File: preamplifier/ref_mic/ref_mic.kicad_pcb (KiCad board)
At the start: 2 copper layers, 49.8 x 9.8 mm, 28 parts, among them U1 OPAMP

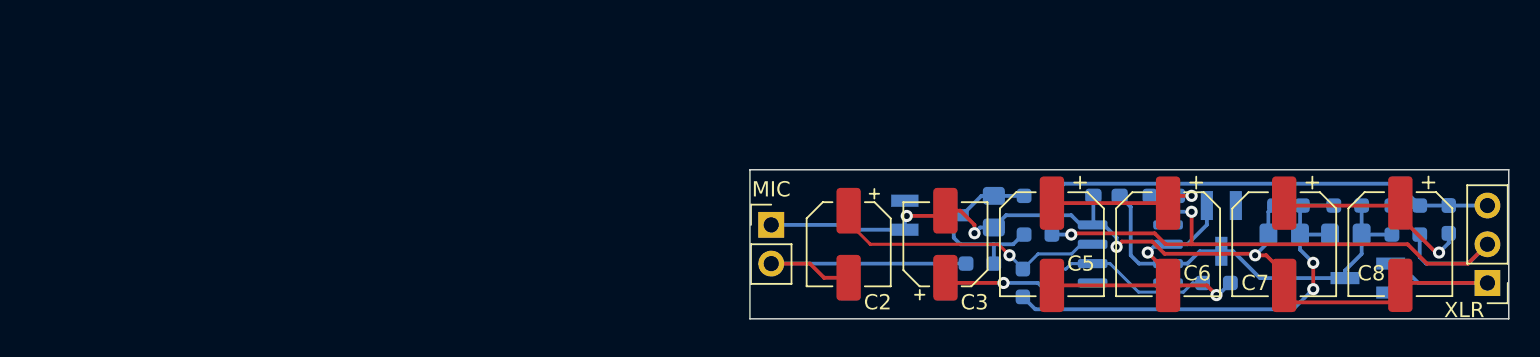
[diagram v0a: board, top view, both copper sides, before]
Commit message: Bulk of v2 updates, before assembly and testing new design - KiCAD project - gerber outputs - schematic PDF - mechanical design (Fusion project, STEP assembly, STL outputs)
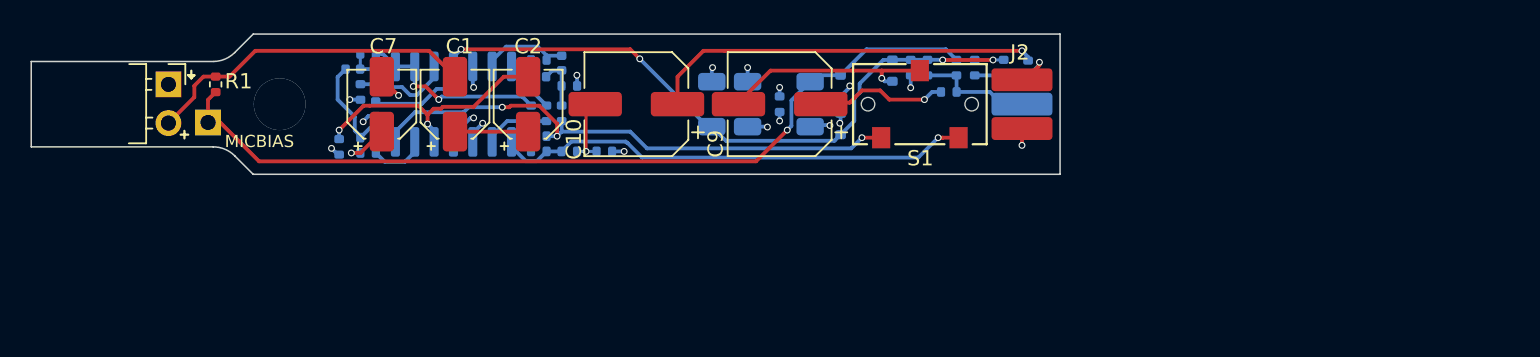
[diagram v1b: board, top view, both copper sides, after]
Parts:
- removed the C8 at (174.6, 110.5)
- removed the D2 at (162.9, 109.5)
- added C1: 4.7uF 35V, Capacitor_SMD:CP_Elec_4x4.5, F.Cu at (112.6, 101.3)
- added C3: 10nF, Capacitor_SMD:C_0402_1005Metric, B.Cu at (105.9, 99.0)
- added C4: 10nF, Capacitor_SMD:C_0402_1005Metric, B.Cu at (107.4, 99.5)
- added C5: 10nF, Capacitor_SMD:C_0402_1005Metric, B.Cu at (118.1, 99.5)
- added D1: D, Diode_SMD:D_SOD-523, B.Cu at (141.3, 99.1)
- added J1: MEMS micbias, Connector_PinHeader_2.54mm:PinHeader_1x01_P2.54mm_Vertical, B.Cu at (96.4, 102.5)
- added R10: 10k, Resistor_SMD:R_0402_1005Metric, B.Cu at (118.1, 103.4)
- added R11: 7.15k, Resistor_SMD:R_0402_1005Metric, B.Cu at (117.6, 101.9)
- added R12: 75k, Resistor_SMD:R_0402_1005Metric, B.Cu at (118.6, 101.9)
- added R13: 10k, Resistor_SMD:R_0402_1005Metric, B.Cu at (118.1, 104.4)
- added R14: 0, Resistor_SMD:R_0402_1005Metric, B.Cu at (120.1, 104.4)
- added R15: 0, Resistor_SMD:R_0402_1005Metric, B.Cu at (122.4, 104.4)
- added R2: 2.94k, Resistor_SMD:R_0402_1005Metric, B.Cu at (119.6, 101.9)
- added R3: 1.74k, Resistor_SMD:R_0402_1005Metric, B.Cu at (120.1, 100.1)
- added R4: 2.67k, Resistor_SMD:R_0402_1005Metric, B.Cu at (106.4, 100.5)
- added R5: 829R, Resistor_SMD:R_0402_1005Metric, B.Cu at (106.9, 98.0)
- added R6: 2.67k, Resistor_SMD:R_0402_1005Metric, B.Cu at (118.1, 98.4)
- added S1: CL-SB-12B-01T, OpenRefMic:CL-SB-12B-01_NDC, F.Cu at (143.1, 101.3)
- C10: renamed from C7; footprint Capacitor_SMD:CP_Elec_6.3x5.4_Nichicon -> Capacitor_SMD:CP_Elec_6.3x4.5
- C11: renamed from C9; footprint Capacitor_SMD:C_0805_2012Metric_Pad1.18x1.45mm_HandSolder -> Capacitor_SMD:C_1206_3216Metric
- C12: renamed from C10; footprint Capacitor_SMD:C_0805_2012Metric_Pad1.18x1.45mm_HandSolder -> Capacitor_SMD:C_1206_3216Metric
- C13: renamed from C1; footprint Capacitor_SMD:C_0805_2012Metric_Pad1.18x1.45mm_HandSolder -> Capacitor_SMD:C_1206_3216Metric
- C2: value 22uF 16V -> 4.7uF 35V; footprint Capacitor_SMD:CP_Elec_5x5.4 -> Capacitor_SMD:CP_Elec_4x4.5
- C6: value 10uF 50v -> 10nF; footprint Capacitor_SMD:CP_Elec_6.3x5.4_Nichicon -> Capacitor_SMD:C_0402_1005Metric; moved to B.Cu
- C7: renamed from C3; value 22uF 16V -> 10uF 16V; footprint Capacitor_SMD:CP_Elec_5x5.4 -> Capacitor_SMD:CP_Elec_4x4.5
- C8: renamed from C4; footprint Capacitor_SMD:C_0603_1608Metric_Pad1.08x0.95mm_HandSolder -> Capacitor_SMD:C_0402_1005Metric
- C9: renamed from C5; footprint Capacitor_SMD:CP_Elec_6.3x5.4_Nichicon -> Capacitor_SMD:CP_Elec_6.3x4.5
- D2: renamed from D3; footprint Package_TO_SOT_SMD:SOT-23_Handsoldering -> Diode_SMD:D_SOD-523
- D3: renamed from D1; footprint Package_TO_SOT_SMD:SC-59_Handsoldering -> Diode_SMD:D_SOD-523
- J2: renamed from XLR; value XLR3 -> Mini XLR Male; footprint Connector_PinHeader_2.54mm:PinHeader_1x03_P2.54mm_Vertical -> OpenRefMic:Switchcraft_T3BM_edgemount
- MK1: renamed from MIC; value Microphone -> AOM-5024L-HD-F-R; footprint Connector_PinHeader_2.54mm:PinHeader_1x02_P2.54mm_Vertical -> Connector_PinSocket_2.54mm:PinSocket_1x02_P2.54mm_Horizontal
- R1: footprint Resistor_SMD:R_0603_1608Metric_Pad0.98x0.95mm_HandSolder -> Resistor_SMD:R_0402_1005Metric; moved to F.Cu
- R16: renamed from R5; footprint Resistor_SMD:R_0603_1608Metric_Pad0.98x0.95mm_HandSolder -> Resistor_SMD:R_0402_1005Metric
- R17: renamed from R6; footprint Resistor_SMD:R_0603_1608Metric_Pad0.98x0.95mm_HandSolder -> Resistor_SMD:R_0402_1005Metric
- R18: renamed from R9; value 10k -> 22k; footprint Resistor_SMD:R_0603_1608Metric_Pad0.98x0.95mm_HandSolder -> Resistor_SMD:R_0402_1005Metric
- R19: renamed from R8; footprint Resistor_SMD:R_0603_1608Metric_Pad0.98x0.95mm_HandSolder -> Resistor_SMD:R_0402_1005Metric
- R20: renamed from R10; value 10k -> 22k; footprint Resistor_SMD:R_0603_1608Metric_Pad0.98x0.95mm_HandSolder -> Resistor_SMD:R_0402_1005Metric
- R21: renamed from R12; footprint Resistor_SMD:R_0603_1608Metric_Pad0.98x0.95mm_HandSolder -> Resistor_SMD:R_0402_1005Metric
- R22: renamed from R7; footprint Resistor_SMD:R_0603_1608Metric_Pad0.98x0.95mm_HandSolder -> Resistor_SMD:R_0402_1005Metric
- R23: renamed from R11; footprint Resistor_SMD:R_0603_1608Metric_Pad0.98x0.95mm_HandSolder -> Resistor_SMD:R_0402_1005Metric
- R7: renamed from R2; footprint Resistor_SMD:R_0603_1608Metric_Pad0.98x0.95mm_HandSolder -> Resistor_SMD:R_0402_1005Metric
- R8: renamed from R3; footprint Resistor_SMD:R_0603_1608Metric_Pad0.98x0.95mm_HandSolder -> Resistor_SMD:R_0402_1005Metric
- R9: renamed from R4; value 10k -> 0; footprint Resistor_SMD:R_0603_1608Metric_Pad0.98x0.95mm_HandSolder -> Resistor_SMD:R_0402_1005Metric
- U1: value OPAMP -> OPA1664; footprint Package_SO:SOIC-8_3.9x4.9mm_P1.27mm -> Package_SO:SO-14_3.9x8.65mm_P1.27mm
- moved R9 56.5 mm to (106.9, 103.5), turned to 180 degrees
- moved R1 51.5 mm to (96.9, 100.0), turned to 90 degrees
- moved C8 48.3 mm to (107.4, 101.6), turned to -90 degrees
- moved R7 45.7 mm to (105.0, 104.1)
- moved R8 45.7 mm to (106.9, 104.5), turned to 180 degrees
- moved U1 45.5 mm to (112.5, 101.3), turned to -90 degrees
- moved C10 43.5 mm to (124.5, 101.3), turned to 180 degrees
- moved C11 42.5 mm to (129.4, 101.3), turned to 90 degrees
- moved C6 41.5 mm to (119.6, 98.6), turned to 90 degrees
- moved MK1 40.6 mm to (93.8, 100.0)
- moved C7 38.1 mm to (107.8, 101.3)
- moved C12 36.2 mm to (131.8, 101.3), turned to -90 degrees
- moved D2 36.0 mm to (137.9, 102.6), turned to 90 degrees
- moved R20 34.0 mm to (133.9, 101.3), turned to -90 degrees
- moved R19 33.2 mm to (143.6, 98.9), turned to 90 degrees
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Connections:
- C10 pad 2: GND -> /OUT-
- C11 pad 1: /Opamp_VDD -> AMP_VDD
- C11 pad 2: /VGND -> VGND
- C12 pad 1: /VGND -> VGND
- C13 pad 1: /Micbias -> MICBIAS
- C2 pad 1: /Opamp_In+ -> Net-(C1-Pad1)
- C2 pad 2: /Mic+ -> /PREAMP_IN
- C6 pad 1: Net-(C5-Pad1) -> /BP_FB
- C6 pad 2: /Opamp_Out -> /BP_IN
- C8 pad 1: /Opamp_VDD -> AMP_VDD
- C9 pad 1: Net-(C5-Pad1) -> Net-(C9-Pad1)
- C9 pad 2: /Opamp_Out -> /OUT+
- D2 pad 1: GND -> AMP_VDD
- D2 pad 2: (no net) -> GND
- D3 pad 1: GND -> MICBIAS
- D3 pad 2: (no net) -> GND
- MK1 pad 2: /Mic+ -> /MIC+
- R1 pad 1: /Micbias -> MICBIAS
- R1 pad 2: /Mic+ -> /MIC+
- R16 pad 1: Net-(C5-Pad1) -> Net-(C9-Pad1)
- R18 pad 1: /Opamp_VDD -> AMP_VDD
- R18 pad 2: /VGND -> VGND
- R19 pad 2: /Opamp_VDD -> AMP_VDD
- R20 pad 1: /VGND -> VGND
- R21 pad 2: /Opamp_VDD -> AMP_VDD
- R22 pad 1: /Micbias -> MICBIAS
- R23 pad 1: /Micbias -> MICBIAS
- R7 pad 1: /Opamp_In+ -> /PREAMP_IN
- R7 pad 2: /VGND -> VGND
- R8 pad 1: /Opamp_In- -> /PREAMP_FB
- R9 pad 1: /Opamp_In- -> /PREAMP_FB
- R9 pad 2: /Opamp_Out -> /PREAMP_OUT
- U1 pad 1: (no net) -> /HP_OUT
- U1 pad 2: /Opamp_In- -> /HP_OUT
- U1 pad 3: /Opamp_In+ -> /HP_IN
- U1 pad 4: GND -> AMP_VDD
- U1 pad 5: (no net) -> VGND
- U1 pad 6: /Opamp_Out -> /BP_IN
- U1 pad 7: /Opamp_VDD -> /BP_OUT
- U1 pad 8: (no net) -> /MIX_OUT
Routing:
- net MICBIAS: track 0.00 -> 58.0 mm, vias 0 -> 1
- net GND: track 65.7 -> 11.6 mm, vias 4 -> 10
- net AMP_VDD: track 0.00 -> 49.7 mm, vias 0 -> 4
- net /PREAMP_OUT: track 0.00 -> 45.4 mm, vias 0 -> 3
- net /XLR2(+): track 41.9 -> 7.62 mm, vias 2 -> 0
- net /MIX_OUT: track 0.00 -> 31.6 mm, vias 0 -> 1
- net /VGND: track 29.9 -> 0.00 mm, vias 2 -> 0
- net /Opamp_VDD: track 28.6 -> 0.00 mm
- net /XLR3(-): track 29.5 -> 6.48 mm, vias 0 -> 1
- net /MIC+: track 0.00 -> 21.9 mm
- net /Opamp_Out: track 20.9 -> 0.00 mm, vias 2 -> 0
- net /Opamp_In+: track 18.7 -> 0.00 mm, vias 1 -> 0
- net /Mic+: track 18.2 -> 0.00 mm
- net /PREAMP_IN: track 0.00 -> 16.9 mm, vias 0 -> 2
- net /OUT+: track 0.00 -> 14.1 mm, vias 0 -> 1
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- added copper zone on In1.Cu, net GND
- added copper zone on In2.Cu, net VGND
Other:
- board size 49.8 x 9.8 mm -> 67.5 x 9.2 mm
- copper layers 2 -> 4
- rule pad_to_mask_clearance: 0 -> 0.05
- board text added: "MICBIAS"
- board text added: "Mic"
- board text added: "Open"
- board text added: "Ref"
- board text added: "v2"

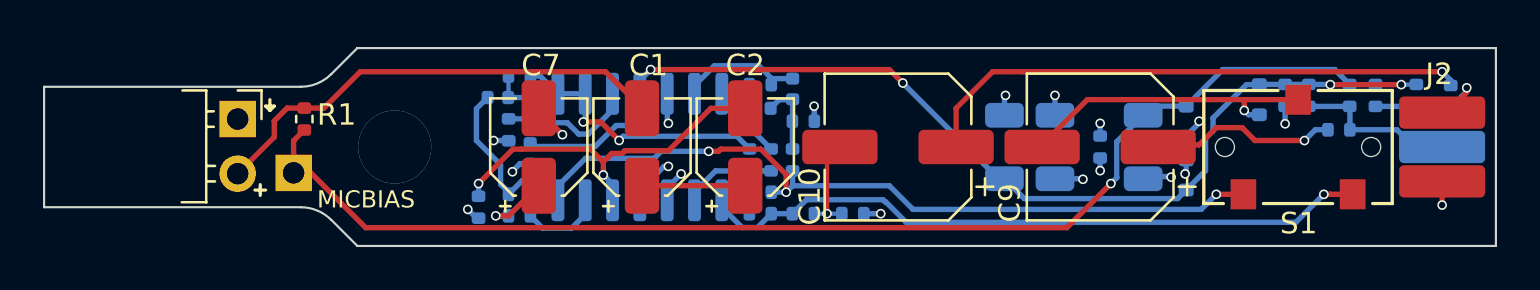
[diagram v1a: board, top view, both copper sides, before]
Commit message: major v2 updates
fixes based on initial v2 PCB build
- R6 corrected to 8.06k
- Replaced opamp with OPA4991
- Adjust phantom power resistor values to optimize opamp Vdd
- Connect R15 to VGND to avoid exceeding C10 voltage rating
- Increase values of input AC-coupling caps, output caps, phantom power caps, decrease output series resistors. Reduces low frequency rolloff
- Add D4 for alternate configs where In- is connected to an opamp output
- Improved PCB layout
- Improved CAD design, add soldering jig
- Add 3MF with print settings for grille and body

Update preamp documentation, add instructions for no/alternate filtering configs
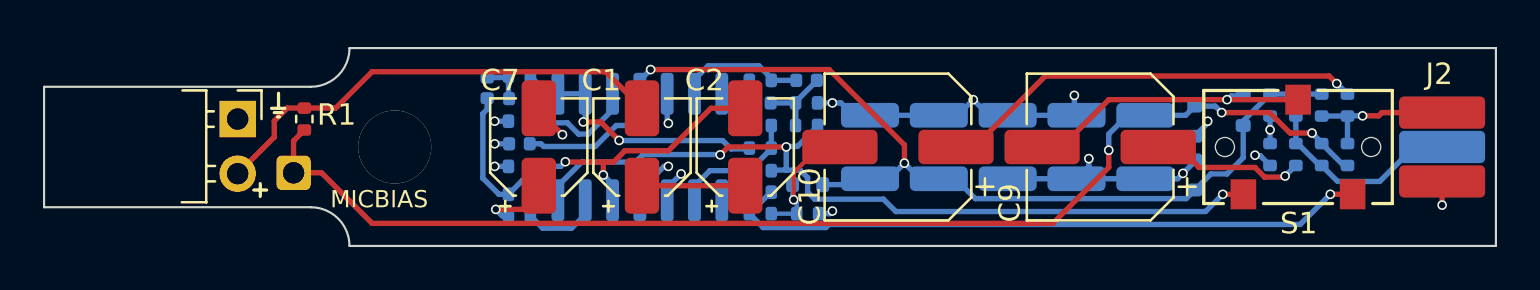
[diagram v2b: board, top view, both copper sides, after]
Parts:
- added C13: 22uF 16V, OpenRefMic:C_1210_3225Metric_0.95mm-height, B.Cu at (123.2, 101.3)
- added C14: 22uF 16V, OpenRefMic:C_1210_3225Metric_0.95mm-height, B.Cu at (132.8, 101.3)
- added D4: 1N4148, Diode_SMD:D_SOD-523, B.Cu at (120.3, 103.0)
- C1, C2: value 4.7uF 35V -> 10uF 16V
- C10, C9: value 10uF 50v -> 22uF 25v
- C11, C12: value 10uF 16V -> 22uF 16V; footprint Capacitor_SMD:C_1206_3216Metric -> OpenRefMic:C_1210_3225Metric_0.95mm-height
- C15: renamed from C13; value 10uF 16V -> 22uF 16V; footprint Capacitor_SMD:C_1206_3216Metric -> OpenRefMic:C_1210_3225Metric_0.95mm-height
- D1: value D -> 1N4148
- D3: value 5V6 -> 5.6V
- J1: footprint Connector_PinHeader_2.54mm:PinHeader_1x01_P2.54mm_Vertical -> Connector_Wire:SolderWire-0.1sqmm_1x01_D0.4mm_OD1mm
- R1, R8: value 4k7 -> 4.7k
- R16, R17: value 100R -> 10R
- R18: renamed from R19; value 4k7 -> 7.15k
- R19: renamed from R21; value 4k7 -> 7.15k
- R20: renamed from R18; value 22k -> 7.15k
- R21: renamed from R20; value 22k -> 7.15k
- R5: value 829R -> 825R
- R6: value 2.67k -> 8.06k
- U1: value OPA1664 -> OPA4991
- moved R21 7.91 mm to (141.8, 101.7)
- moved R17 4.82 mm to (145.4, 99.3)
- moved R19 4.42 mm to (144.2, 99.3)
- moved C11 3.05 mm to (126.4, 101.3)
- moved R22 3.04 mm to (144.2, 101.7)
- moved R23 3.04 mm to (145.4, 101.7), turned to 90 degrees
- moved R7 2.69 mm to (106.9, 102.2), turned to 180 degrees
- moved R16 2.31 mm to (143.0, 101.7), turned to 90 degrees
- moved C12 2.20 mm to (129.6, 101.3)
- moved R15 2.10 mm to (120.3, 104.4)
- moved R14 2.00 mm to (118.1, 104.4)
- moved R2 1.73 mm to (120.2, 100.3), turned to 180 degrees
- moved R12 1.68 mm to (118.1, 100.3), turned to 0 degrees
- moved R10 1.00 mm to (118.1, 102.4)
- moved R13 1.00 mm to (118.1, 103.4)
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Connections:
- R15 pad 2: GND -> VGND
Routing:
- net VGND: track 8.25 -> 20.0 mm
- net GND: track 11.6 -> 18.0 mm, vias 10 -> 8
- net Net-(C10-Pad1): track 25.9 -> 19.9 mm
- net /PREAMP_IN: track 16.9 -> 13.1 mm
- net /OUT-: track 5.53 -> 7.41 mm
- net /XLR2(+): track 7.62 -> 9.47 mm
- net /PREAMP_OUT: track 45.4 -> 47.2 mm
- net MICBIAS: track 58.0 -> 56.4 mm, vias 1 -> 3
- net /BP_OUT: track 5.00 -> 3.59 mm
- net Net-(C9-Pad1): track 8.68 -> 7.30 mm
- net /MIX_OUT: track 31.6 -> 32.3 mm
- net /MIX_IN: track 6.34 -> 7.03 mm
- net AMP_VDD: track 49.7 -> 49.9 mm, vias 4 -> 2
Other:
- outline, holes or cut-outs redrawn

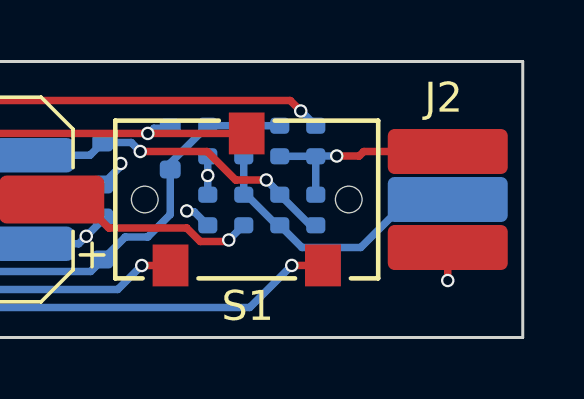
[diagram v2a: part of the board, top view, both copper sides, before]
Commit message: major v2 updates
Likely the final versions of v2 design files
- updated CAD. Small tweaks to spacers, modeled in grille openings (instead of relying on slicer settings), increased room for taller caps, increased clearance for header pins on bottom of PCB
- Updated EQ component values based on measurements of several prototypes (original v1 prototype capsule response deviated significantly from other 5+ other capsules tested).
- Added PCB thickness requirement note to preamp doc and directly on fab layer of layout
- Updated all KiCAD files, gerber outputs, schematic outputs, etc.
- updated readme, preamp docs
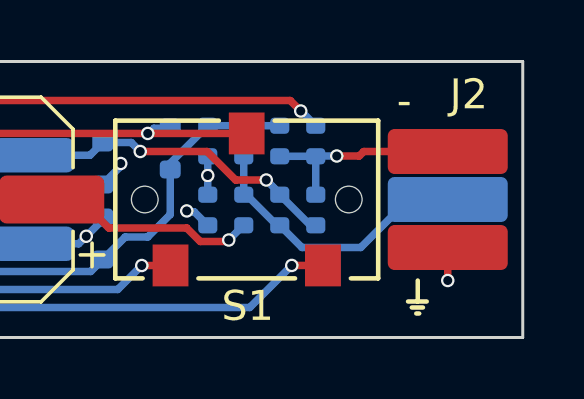
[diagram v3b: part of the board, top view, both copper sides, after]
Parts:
- R16, R17: value 10R -> 100R
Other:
- board text added: "+"
- board text added: "-"
- board text added: "0.010mm 0.035mm 0.210mm 0.015mm 0.600mm 0.015mm 0.210mm 0.035mm 0.010mm"
- board text added: "1.2mm total"
- board text added: "Maximum board thickness: 1.5mm Typical stackup:"
- board text added: "Top Silkscreen Top Solder Paste Top Solder Mask Top Copper - Signal Prepreg Inner Copper 1 - GND Core Inner Copper 2 - VGND Prepreg Bottom Copper - Signal Bottom Solder Mask Bottom Solder Paste Bottom Silkscreen"
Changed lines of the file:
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@@
 		(tenting front back)
 		(pcbplotparams
-			(layerselection 0x00000000_00000000_55555555_5755f5ff)
+			(layerselection 0x00000000_00000000_5555555f_5755f5ff)
 			(plot_on_all_layers_selection 0x00000000_00000000_00000000_00000000)
 			(disableapertmacros no)
@@
 			)
 		)
-		(property "LCSC_Part_Number" ""
+		(property "LCSC_Part_Number" "Nichicon UZG1E220MCL1GB"
 			(at 0 0 180)
 			(unlocked yes)
@@
 			)
 		)
-		(property "LCSC_Part_Number" ""
+		(property "LCSC_Part_Number" "Nichicon UZG1E220MCL1GB"
 			(at 0 0 180)
 			(unlocked yes)
@@
 		(at 152.3 101.3)
 		(property "Reference" "J2"
-			(at -2.64 -3.39 0)
+			(at -1.8 -3.5 0)
 			(unlocked yes)
 			(layer "F.SilkS")
@@
 			)
 		)
-		(property "LCSC_Part_Number" ""
+		(property "LCSC_Part_Number" "Taiyo Yuden EMK325BJ226MD-T"
 			(at 0 0 270)
 			(unlocked yes)
@@
 			)
 		)
-		(property "Value" "10R"
+		(property "Value" "100R"
 			(at 0 -1.17 90)
 			(layer "B.Fab")
@@
 			)
 		)
-		(property "LCSC_Part_Number" ""
+		(property "LCSC_Part_Number" "YAGEO RC0402FR-07100RL"
 			(at 0 0 270)
 			(unlocked yes)
@@
 			)
 		)
-		(property "DigiKey_Part_Number" "RC0402FR-0710RL"
+		(property "DigiKey_Part_Number" "RC0402FR-07100RL"
 			(at 0 0 270)
 			(unlocked yes)
@@
 			)
 		)
-		(property "LCSC_Part_Number" ""
+		(property "LCSC_Part_Number" "TI OPA4991IDR"
 			(at 0 0 90)
 			(unlocked yes)
@@
 			)
 		)
-		(property "LCSC_Part_Number" ""
+		(property "LCSC_Part_Number" "YAGEO AC0402FR-078K06L"
 			(at 0 0 0)
 			(unlocked yes)
@@
 			)
 		)
-		(property "LCSC_Part_Number" ""
+		(property "LCSC_Part_Number" "Taiyo Yuden EMK325BJ226MD-T"
 			(at 0 0 270)
 			(unlocked yes)
@@
 			)
 		)
-		(property "LCSC_Part_Number" ""
+		(property "LCSC_Part_Number" "Taiyo Yuden EMK325BJ226MD-T"
 			(at 0 0 90)
 			(unlocked yes)
@@
 			)
 		)
-		(property "LCSC_Part_Number" ""
+		(property "LCSC_Part_Number" "Taiyo Yuden EMK325BJ226MD-T"
 			(at 0 0 90)
 			(unlocked yes)
@@
 			)
 		)
-		(property "LCSC_Part_Number" "YAGEO RC0402FR-077K15L"
+		(property "LCSC_Part_Number" "YAGEO RC0402FR-074K7L"
 			(at 0 0 180)
 			(unlocked yes)
@@
 			)
 		)
-		(property "LCSC_Part_Number" ""
+		(property "LCSC_Part_Number" "Taiyo Yuden EMK325BJ226MD-T"
 			(at 0 0 270)
 			(unlocked yes)
@@
 			)
 		)
-		(property "Value" "10R"
+		(property "Value" "100R"
 			(at 0 -1.17 90)
 			(layer "B.Fab")
@@
 			)
 		)
-		(property "LCSC_Part_Number" ""
+		(property "LCSC_Part_Number" "YAGEO RC0402FR-07100RL"
 			(at 0 0 90)
 			(unlocked yes)
@@
 			)
 		)
-		(property "DigiKey_Part_Number" "RC0402FR-0710RL"
+		(property "DigiKey_Part_Number" "RC0402FR-07100RL"
 			(at 0 0 90)
 			(unlocked yes)
@@
 	)
 	(gr_line
+		(start 148.75 105.1)
+		(end 148.85 105.1)
+		(stroke
+			(width 0.15)
+			(type default)
+		)
+		(layer "F.SilkS")
+	)
+	(gr_line
+		(start 149.1 104.7)
+		(end 148.475 104.7)
+		(stroke
+			(width 0.15)
+			(type default)
+		)
+		(layer "F.SilkS")
+	)
+	(gr_line
 		(start 95.7 98.8)
 		(end 95.7 99.5)
@@
 	)
 	(gr_line
+		(start 148.6 104.9)
+		(end 148.975 104.9)
+		(stroke
+			(width 0.15)
+			(type default)
+		)
+		(layer "F.SilkS")
+	)
+	(gr_line
 		(start 96 99.5)
 		(end 95.375 99.5)
@@
 		(layer "F.SilkS")
 	)
+	(gr_line
+		(start 148.8 104)
+		(end 148.8 104.7)
+		(stroke
+			(width 0.15)
+			(type default)
+		)
+		(layer "F.SilkS")
+	)
 	(gr_poly
 		(pts
@@
 		(layer "F.CrtYd")
 	)
+	(gr_line
+		(start 119 92.5)
+		(end 121 92.5)
+		(stroke
+			(width 0.15)
+			(type default)
+		)
+		(layer "F.Fab")
+	)
+	(gr_line
+		(start 120 71)
+		(end 120 92.5)
+		(stroke
+			(width 0.15)
+			(type default)
+		)
+		(layer "F.Fab")
+	)
+	(gr_line
+		(start 119 71)
+		(end 121 71)
+		(stroke
+			(width 0.15)
+			(type default)
+		)
+		(layer "F.Fab")
+	)
 	(gr_text "MICBIAS"
 		(at 98.1 104.2 0)
@@
 		)
 	)
+	(gr_text "-"
+		(at 148.1 98.6 0)
+		(layer "F.SilkS")
+		(effects
+			(font
+				(size 1 1)
+				(thickness 0.15)
+			)
+			(justify left bottom)
+		)
+	)
 	(gr_text "Mic"
 		(at 92 103.82 0)
@@
 		)
 	)
+	(gr_text "+"
+		(at 149.3 100.2 0)
+		(layer "B.SilkS")
+		(effects
+			(font
+				(size 1 1)
+				(thickness 0.15)
+			)
+			(justify left bottom)
+		)
+	)
 	(gr_text "v2"
 		(at 87.05 103.67 0)
@@
 		)
 	)
+	(gr_text "1.2mm total"
+		(at 109.25 71.75 0)
+		(layer "F.Fab")
+		(effects
+			(font
+				(size 1 1)
+				(thickness 0.15)
+			)
+			(justify left bottom)
+		)
+	)
+	(gr_text "Top Silkscreen\nTop Solder Paste\nTop Solder Mask\nTop Copper - Signal\nPrepreg\nInner Copper 1 - GND\nCore\nInner Copper 2 - VGND\nPrepreg\nBottom Copper - Signal\nBottom Solder Mask\nBottom Solder Paste\nBottom Silkscreen"
+		(at 121 92 0)
+		(layer "F.Fab")
+		(effects
+			(font
+				(size 1 1)
+				(thickness 0.15)
+			)
+			(justify left bottom)
+		)
+	)
+	(gr_text "\n\n0.010mm\n0.035mm\n0.210mm\n0.015mm\n0.600mm\n0.015mm\n0.210mm\n0.035mm\n0.010mm"
+		(at 119 88.75 0)
+		(layer "F.Fab")
+		(effects
+			(font
+				(size 1 1)
+				(thickness 0.15)
+			)
+			(justify right bottom)
+		)
+	)
+	(gr_text "Maximum board thickness: 1.5mm\nTypical stackup:"
+		(at 109 69.25 0)
+		(layer "F.Fab")
+		(effects
+			(font
+				(size 1.5 1.5)
+				(thickness 0.2)
+			)
+			(justify left bottom)
+		)
+	)
